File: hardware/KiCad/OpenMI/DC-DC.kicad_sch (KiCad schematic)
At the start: 37 parts, among them Q4 GAN7R0-150LBEZ, Q5 GAN7R0-150LBEZ, U3 1EDN7550B, U4 1EDN7550B

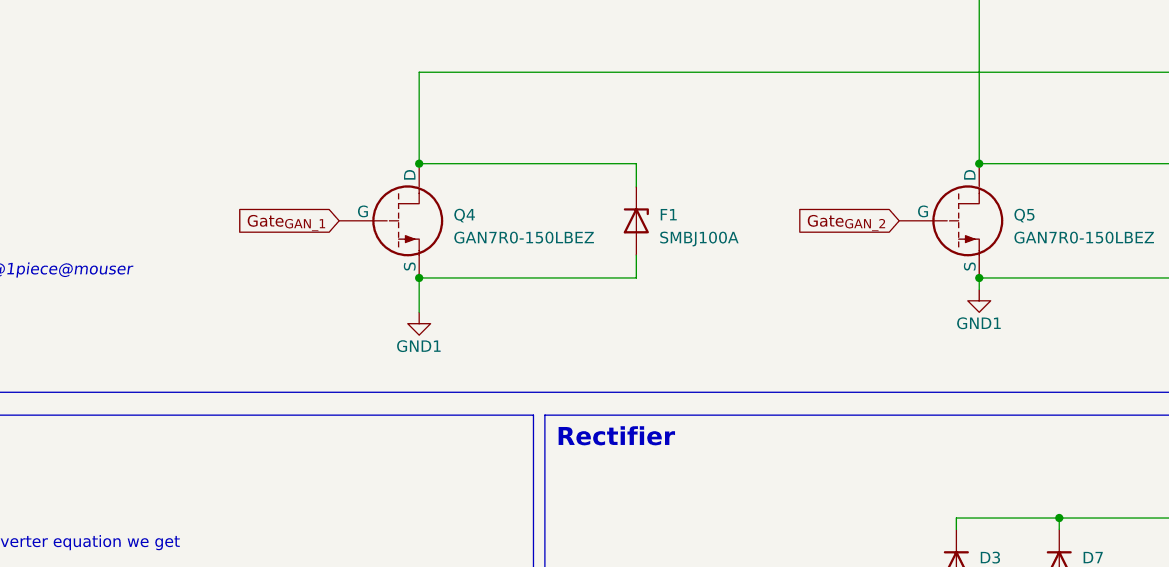
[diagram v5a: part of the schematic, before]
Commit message: feat(hw): adds safety resistors to gate of GaN FET
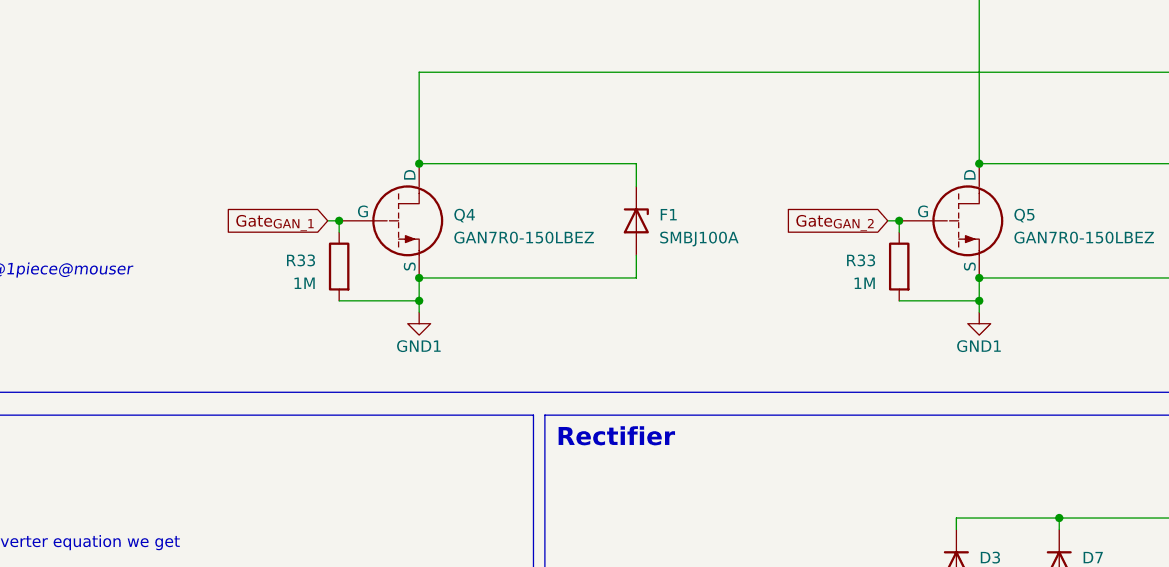
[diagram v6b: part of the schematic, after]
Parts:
- added R33 (x2): 1M, Resistor_SMD:R_0603_1608Metric, symbol _R_0603:1M
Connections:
- net GND1: now also R33.2, R33.2
- net Gate_{GAN_1}: now also R33.1
- net Gate_{GAN_2}: now also R33.1
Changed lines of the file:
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@@
   (junction (at 62.865 74.295) (diameter 0) (color 0 0 0 0)
   )
+  (junction (at 308.61 151.13) (diameter 0) (color 0 0 0 0)
+  )
   (junction (at 287.02 27.94) (diameter 0) (color 0 0 0 0)
   )
@@
   (junction (at 246.38 135.89) (diameter 0) (color 0 0 0 0)
   )
+  (junction (at 237.49 142.24) (diameter 0) (color 0 0 0 0)
+  )
   (junction (at 62.865 66.675) (diameter 0) (color 0 0 0 0)
   )
@@
   (junction (at 308.61 148.59) (diameter 0) (color 0 0 0 0)
   )
+  (junction (at 299.72 142.24) (diameter 0) (color 0 0 0 0)
+  )
   (junction (at 317.5 175.26) (diameter 0) (color 0 0 0 0)
   )
+  (junction (at 246.38 151.13) (diameter 0) (color 0 0 0 0)
+  )
   (junction (at 32.385 66.675) (diameter 0) (color 0 0 0 0)
   )
-  (wire (pts (xy 246.38 152.4) (xy 246.38 148.59))
+  (wire (pts (xy 308.61 152.4) (xy 308.61 151.13))
+    (stroke (width 0) (type default))
+  )
+  (wire (pts (xy 246.38 151.13) (xy 246.38 148.59))
+    (stroke (width 0) (type default))
+  )
+  (wire (pts (xy 246.38 152.4) (xy 246.38 151.13))
     (stroke (width 0) (type default))
   )
@@
     (stroke (width 0) (type default))
   )
+  (wire (pts (xy 236.22 142.24) (xy 237.49 142.24))
+    (stroke (width 0) (type default))
+  )
   (wire (pts (xy 265.43 90.17) (xy 275.59 90.17))
     (stroke (width 0) (type default))
@@
     (stroke (width 0) (type default))
   )
+  (wire (pts (xy 237.49 142.24) (xy 237.49 143.51))
+    (stroke (width 0) (type default))
+  )
   (wire (pts (xy 62.865 90.17) (xy 78.105 90.17))
     (stroke (width 0) (type default))
   )
+  (wire (pts (xy 298.45 142.24) (xy 299.72 142.24))
+    (stroke (width 0) (type default))
+  )
   (wire (pts (xy 331.47 175.26) (xy 331.47 184.15))
     (stroke (width 0) (type default))
@@
     (stroke (width 0) (type default))
   )
+  (wire (pts (xy 299.72 151.13) (xy 308.61 151.13))
+    (stroke (width 0) (type default))
+  )
   (wire (pts (xy 292.1 190.5) (xy 317.5 190.5))
     (stroke (width 0) (type default))
@@
     (stroke (width 0) (type default))
   )
+  (wire (pts (xy 237.49 151.13) (xy 246.38 151.13))
+    (stroke (width 0) (type default))
+  )
   (wire (pts (xy 311.15 50.8) (xy 317.5 50.8))
     (stroke (width 0) (type default))
@@
     (stroke (width 0) (type default))
   )
-  (wire (pts (xy 308.61 148.59) (xy 308.61 149.86))
+  (wire (pts (xy 308.61 148.59) (xy 308.61 151.13))
     (stroke (width 0) (type default))
   )
@@
   )
   (wire (pts (xy 47.625 74.295) (xy 62.865 74.295))
+    (stroke (width 0) (type default))
+  )
+  (wire (pts (xy 299.72 142.24) (xy 299.72 143.51))
     (stroke (width 0) (type default))
   )
@@
     )
   )
-  (global_label "Gate_{GAN_2}" (shape input) (at 299.72 142.24 180) (fields_autoplaced)
+  (global_label "Gate_{GAN_2}" (shape input) (at 298.45 142.24 180) (fields_autoplaced)
     (effects (font (size 1.27 1.27)) (justify right))
-    (property "Intersheetrefs" "${INTERSHEET_REFS}" (at 288.3984 142.24 0)
+    (property "Intersheetrefs" "${INTERSHEET_REFS}" (at 287.1284 142.24 0)
       (effects (font (size 1.27 1.27)) (justify right) hide)
     )
@@
     )
   )
-  (global_label "Gate_{GAN_1}" (shape input) (at 237.49 142.24 180) (fields_autoplaced)
+  (global_label "Gate_{GAN_1}" (shape input) (at 236.22 142.24 180) (fields_autoplaced)
     (effects (font (size 1.27 1.27)) (justify right))
-    (property "Intersheetrefs" "${INTERSHEET_REFS}" (at 226.1684 142.24 0)
+    (property "Intersheetrefs" "${INTERSHEET_REFS}" (at 224.8984 142.24 0)
       (effects (font (size 1.27 1.27)) (justify right) hide)
     )
@@
     )
   )
-  (symbol (lib_id "power:GND1") (at 308.61 149.86 0) (unit 1)
+  (symbol (lib_id "power:GND1") (at 308.61 152.4 0) (unit 1)
     (in_bom yes) (on_board yes) (dnp no)
-    (property "Reference" "#PWR028" (at 308.61 156.21 0)
-      (effects (font (size 1.27 1.27)) hide)
-    )
-    (property "Value" "GND1" (at 308.61 153.67 0)
-      (effects (font (size 1.27 1.27)))
-    )
-    (property "Footprint" "" (at 308.61 149.86 0)
-      (effects (font (size 1.27 1.27)) hide)
-    )
-    (property "Datasheet" "" (at 308.61 149.86 0)
+    (property "Reference" "#PWR028" (at 308.61 158.75 0)
+      (effects (font (size 1.27 1.27)) hide)
+    )
+    (property "Value" "GND1" (at 308.61 156.21 0)
+      (effects (font (size 1.27 1.27)))
+    )
+    (property "Footprint" "" (at 308.61 152.4 0)
+      (effects (font (size 1.27 1.27)) hide)
+    )
+    (property "Datasheet" "" (at 308.61 152.4 0)
       (effects (font (size 1.27 1.27)) hide)
     )
@@
     )
   )
+  (symbol (lib_id "_R_0603:1M") (at 299.72 147.32 0) (mirror y) (unit 1)
+    (in_bom yes) (on_board yes) (dnp no)
+    (property "Reference" "R33" (at 297.18 146.685 0)
+      (effects (font (size 1.27 1.27)) (justify left))
+    )
+    (property "Value" "1M" (at 297.18 149.225 0)
+      (effects (font (size 1.27 1.27)) (justify left))
+    )
+    (property "Footprint" "Resistor_SMD:R_0603_1608Metric" (at 301.498 147.32 90)
+      (effects (font (size 1.27 1.27)) hide)
+    )
+    (property "Datasheet" "~" (at 299.72 147.32 0)
+      (effects (font (size 1.27 1.27)) hide)
+    )
+    (property "MF" "" (at 299.72 147.32 0)
+      (effects (font (size 1.27 1.27)) hide)
+    )
+    (property "MPN" "" (at 299.72 147.32 0)
+      (effects (font (size 1.27 1.27)) hide)
+    )
+    (property "OC_CONRAD" "" (at 299.72 147.32 0)
+      (effects (font (size 1.27 1.27)) hide)
+    )
+    (property "OC_FARNELL" "" (at 299.72 147.32 0)
+      (effects (font (size 1.27 1.27)) hide)
+    )
+    (property "OC_MOUSER" "603-AC0603FR-071ML" (at 299.72 147.32 0)
+      (effects (font (size 1.27 1.27)) hide)
+    )
+    (property "OC_REICHELT" "" (at 299.72 147.32 0)
+      (effects (font (size 1.27 1.27)) hide)
+    )
+    (pin "1")
+    (pin "2")
+    (instances
+      (project "OpenMI"
+        (path "/2d959e19-1572-42a0-a8fd-da8463ad4e66/19323a41-9b99-4de4-bfae-f2f828815be3"
+          (reference "R33") (unit 1)
+        )
+        (path "/2d959e19-1572-42a0-a8fd-da8463ad4e66/efbfb180-c2bb-45aa-ab04-e5a4cb37fddc"
+          (reference "R37") (unit 1)
+        )
+      )
+    )
+  )
   (symbol (lib_name "33K_2") (lib_id "_R_0603:33K") (at 279.4 50.8 90) (unit 1)
     (in_bom yes) (on_board yes) (dnp no)
@@
         )
       )
+    )
+  )
+  (symbol (lib_id "_R_0603:1M") (at 237.49 147.32 0) (mirror y) (unit 1)
+    (in_bom yes) (on_board yes) (dnp no)
+    (property "Reference" "R33" (at 234.95 146.685 0)
+      (effects (font (size 1.27 1.27)) (justify left))
+    )
+    (property "Value" "1M" (at 234.95 149.225 0)
+      (effects (font (size 1.27 1.27)) (justify left))
+    )
+    (property "Footprint" "Resistor_SMD:R_0603_1608Metric" (at 239.268 147.32 90)
+      (effects (font (size 1.27 1.27)) hide)
+    )
+    (property "Datasheet" "~" (at 237.49 147.32 0)
+      (effects (font (size 1.27 1.27)) hide)
+    )
+    (property "MF" "" (at 237.49 147.32 0)
+      (effects (font (size 1.27 1.27)) hide)
+    )
+    (property "MPN" "" (at 237.49 147.32 0)
+      (effects (font (size 1.27 1.27)) hide)
+    )
+    (property "OC_CONRAD" "" (at 237.49 147.32 0)
+      (effects (font (size 1.27 1.27)) hide)
+    )
+    (property "OC_FARNELL" "" (at 237.49 147.32 0)
+      (effects (font (size 1.27 1.27)) hide)
+    )
+    (property "OC_MOUSER" "603-AC0603FR-071ML" (at 237.49 147.32 0)
+      (effects (font (size 1.27 1.27)) hide)
+    )
+    (property "OC_REICHELT" "" (at 237.49 147.32 0)
+      (effects (font (size 1.27 1.27)) hide)
+    )
+    (pin "1")
+    (pin "2")
+    (instances
+      (project "OpenMI"
+        (path "/2d959e19-1572-42a0-a8fd-da8463ad4e66/19323a41-9b99-4de4-bfae-f2f828815be3"
+          (reference "R33") (unit 1)
+        )
+        (path "/2d959e19-1572-42a0-a8fd-da8463ad4e66/efbfb180-c2bb-45aa-ab04-e5a4cb37fddc"
+          (reference "R36") (unit 1)
+        )
+      )

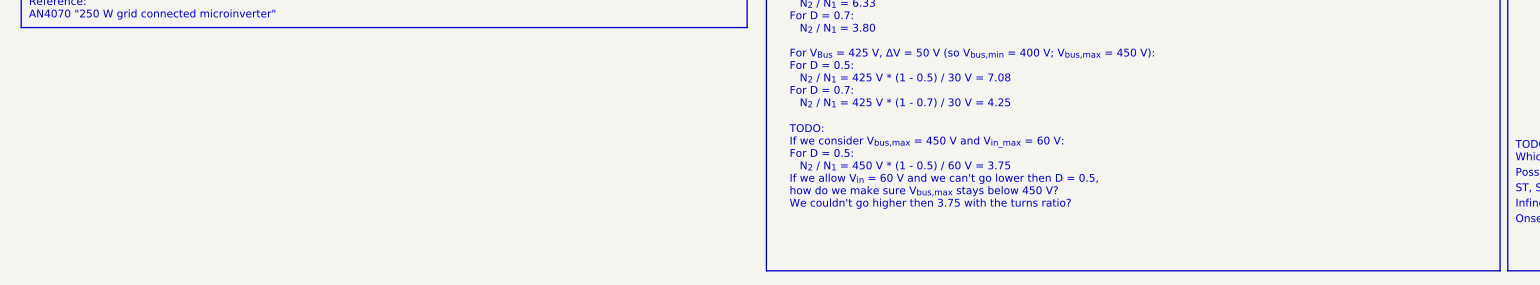
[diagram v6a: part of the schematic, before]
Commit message: chore: sync library for DC-DC schematic
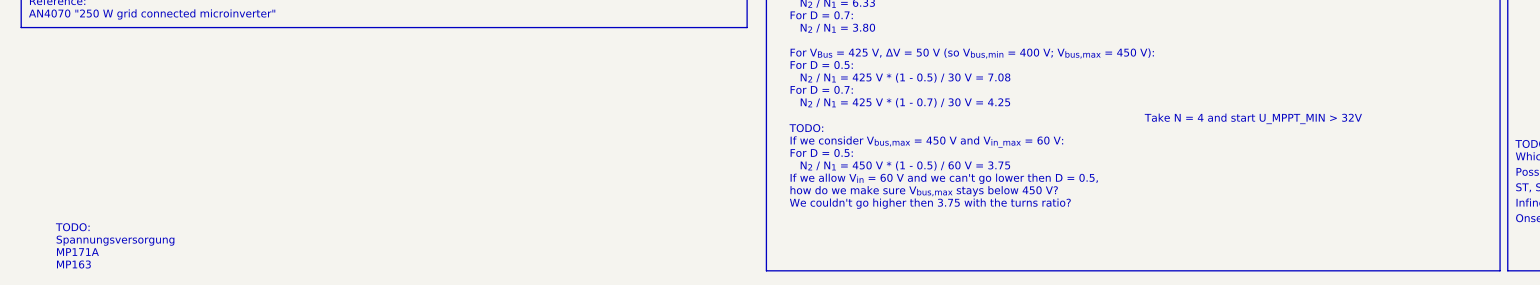
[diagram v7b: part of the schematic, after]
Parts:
- L3, L4, L5, L6, L7, L8: MF 60B104C -> Murata; MPN (none) -> 60B104C; OC_MOUSER 580-60B104C -> 580-60B104C
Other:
- note added: "TODO: Spannungsversorgung MP171A MP163"
- note added: "Take N = 4 and start U_MPPT_MIN > 32V"
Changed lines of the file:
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@@
     (effects (font (size 1.27 1.27) (thickness 0.254) bold) (justify left bottom))
+  )
+  (text "Take N = 4 and start U_MPPT_MIN > 32V" (at 200.66 212.09 0)
+    (effects (font (size 1.27 1.27) (color 255 0 0 1)) (justify left bottom))
   )
   (text "TODO:\nCapacitor size?" (at 340.36 190.5 0)
@@
     (at 18.415 23.495 0)
     (effects (font (size 1.27 1.27)) (justify left bottom))
+  )
+  (text "TODO:\nSpannungsversorgung\nMP171A \nMP163" (at 21.59 236.22 0)
+    (effects (font (size 1.27 1.27)) (justify left bottom) (href "https://www.monolithicpower.com/en/products/power-management/switching-converters-controllers/step-down-buck/converters/vin-max-48v.html"))
   )
   (text "Considerations about possible GaN FET driver:" (at 140.97 81.28 0)
@@
     )
   )
-  (symbol (lib_name "33K_1") (lib_id "_R_0603:33K") (at 279.4 45.72 90) (unit 1)
+  (symbol (lib_id "_R_0603:33K") (at 279.4 45.72 90) (unit 1)
     (in_bom yes) (on_board yes) (dnp no) (fields_autoplaced)
     (property "Reference" "R23" (at 279.4 40.64 90)
@@
       (effects (font (size 1.27 1.27)) hide)
     )
-    (property "MF" "60B104C" (at 105.41 123.19 0)
-      (effects (font (size 1.27 1.27)) hide)
-    )
-    (property "MPN" "" (at 105.41 123.19 0)
+    (property "MF" "Murata" (at 105.41 123.19 0)
+      (effects (font (size 1.27 1.27)) hide)
+    )
+    (property "MPN" "60B104C" (at 105.41 123.19 0)
       (effects (font (size 1.27 1.27)) hide)
     )
@@
       (effects (font (size 1.27 1.27)) hide)
     )
-    (property "OC_MOUSER" " 580-60B104C" (at 105.41 123.19 0)
+    (property "OC_MOUSER" "580-60B104C" (at 105.41 123.19 0)
       (effects (font (size 1.27 1.27)) hide)
     )
@@
       (effects (font (size 1.27 1.27)) hide)
     )
-    (property "MF" "60B104C" (at 119.38 113.665 0)
-      (effects (font (size 1.27 1.27)) hide)
-    )
-    (property "MPN" "" (at 119.38 113.665 0)
+    (property "MF" "Murata" (at 119.38 113.665 0)
+      (effects (font (size 1.27 1.27)) hide)
+    )
+    (property "MPN" "60B104C" (at 119.38 113.665 0)
       (effects (font (size 1.27 1.27)) hide)
     )
@@
       (effects (font (size 1.27 1.27)) hide)
     )
-    (property "OC_MOUSER" " 580-60B104C" (at 119.38 113.665 0)
+    (property "OC_MOUSER" "580-60B104C" (at 119.38 113.665 0)
       (effects (font (size 1.27 1.27)) hide)
     )
@@
     )
   )
-  (symbol (lib_name "33K_2") (lib_id "_R_0603:33K") (at 279.4 50.8 90) (unit 1)
+  (symbol (lib_id "_R_0603:33K") (at 279.4 50.8 90) (unit 1)
     (in_bom yes) (on_board yes) (dnp no)
     (property "Reference" "R24" (at 279.4 53.34 90)
@@
     )
   )
-  (symbol (lib_name "33K_3") (lib_id "_R_0603:33K") (at 279.4 90.17 90) (unit 1)
+  (symbol (lib_id "_R_0603:33K") (at 279.4 90.17 90) (unit 1)
     (in_bom yes) (on_board yes) (dnp no) (fields_autoplaced)
     (property "Reference" "R27" (at 279.4 85.09 90)
@@
       (effects (font (size 1.27 1.27)) hide)
     )
-    (property "MF" "60B104C" (at 91.44 113.665 0)
-      (effects (font (size 1.27 1.27)) hide)
-    )
-    (property "MPN" "" (at 91.44 113.665 0)
+    (property "MF" "Murata" (at 91.44 113.665 0)
+      (effects (font (size 1.27 1.27)) hide)
+    )
+    (property "MPN" "60B104C" (at 91.44 113.665 0)
       (effects (font (size 1.27 1.27)) hide)
     )
@@
       (effects (font (size 1.27 1.27)) hide)
     )
-    (property "OC_MOUSER" " 580-60B104C" (at 91.44 113.665 0)
+    (property "OC_MOUSER" "580-60B104C" (at 91.44 113.665 0)
       (effects (font (size 1.27 1.27)) hide)
     )
@@
       (effects (font (size 1.27 1.27)) hide)
     )
-    (property "MF" "60B104C" (at 119.38 123.19 0)
-      (effects (font (size 1.27 1.27)) hide)
-    )
-    (property "MPN" "" (at 119.38 123.19 0)
+    (property "MF" "Murata" (at 119.38 123.19 0)
+      (effects (font (size 1.27 1.27)) hide)
+    )
+    (property "MPN" "60B104C" (at 119.38 123.19 0)
       (effects (font (size 1.27 1.27)) hide)
     )
@@
       (effects (font (size 1.27 1.27)) hide)
     )
-    (property "OC_MOUSER" " 580-60B104C" (at 119.38 123.19 0)
+    (property "OC_MOUSER" "580-60B104C" (at 119.38 123.19 0)
       (effects (font (size 1.27 1.27)) hide)
     )
@@
     )
   )
-  (symbol (lib_name "33K_4") (lib_id "_R_0603:33K") (at 279.4 95.25 90) (unit 1)
+  (symbol (lib_id "_R_0603:33K") (at 279.4 95.25 90) (unit 1)
     (in_bom yes) (on_board yes) (dnp no)
     (property "Reference" "R28" (at 279.4 97.79 90)
@@
       (effects (font (size 1.27 1.27)) hide)
     )
-    (property "MF" "60B104C" (at 91.44 123.19 0)
-      (effects (font (size 1.27 1.27)) hide)
-    )
-    (property "MPN" "" (at 91.44 123.19 0)
+    (property "MF" "Murata" (at 91.44 123.19 0)
+      (effects (font (size 1.27 1.27)) hide)
+    )
+    (property "MPN" "60B104C" (at 91.44 123.19 0)
       (effects (font (size 1.27 1.27)) hide)
     )
@@
       (effects (font (size 1.27 1.27)) hide)
     )
-    (property "OC_MOUSER" " 580-60B104C" (at 91.44 123.19 0)
+    (property "OC_MOUSER" "580-60B104C" (at 91.44 123.19 0)
       (effects (font (size 1.27 1.27)) hide)
     )
@@
       (effects (font (size 1.27 1.27)) hide)
     )
-    (property "MF" "60B104C" (at 105.41 113.665 0)
-      (effects (font (size 1.27 1.27)) hide)
-    )
-    (property "MPN" "" (at 105.41 113.665 0)
+    (property "MF" "Murata" (at 105.41 113.665 0)
+      (effects (font (size 1.27 1.27)) hide)
+    )
+    (property "MPN" "60B104C" (at 105.41 113.665 0)
       (effects (font (size 1.27 1.27)) hide)
     )
@@
       (effects (font (size 1.27 1.27)) hide)
     )
-    (property "OC_MOUSER" " 580-60B104C" (at 105.41 113.665 0)
-      (effects (font (size 1.27 1.27)) hide)
-    )
+    (property "OC_MOUSER" "580-60B104C" (at 105.41 113.665 0)
+      (effects (font (size 1.27 1.27)) hide)
+    )

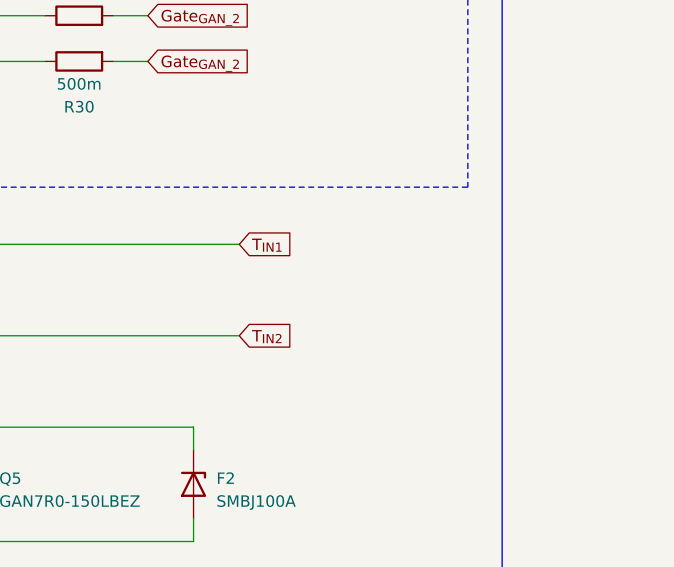
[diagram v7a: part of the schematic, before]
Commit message: docs(hw): adds todo on where to place transformer in schematic
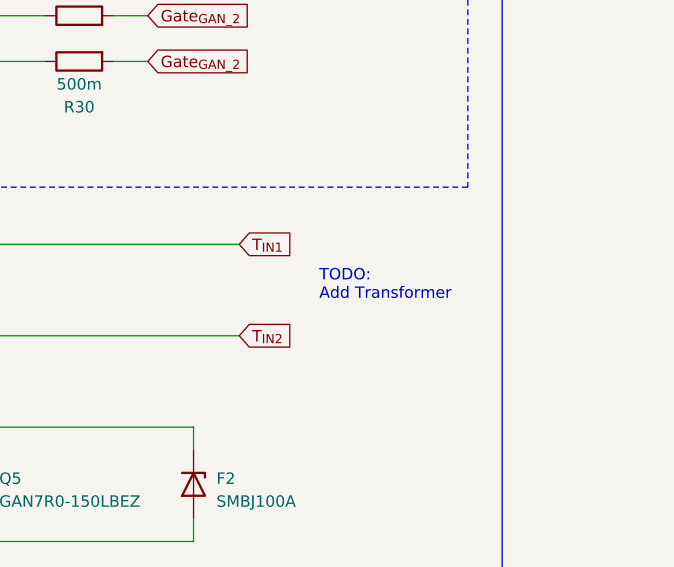
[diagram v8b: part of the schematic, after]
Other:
- note added: "TODO: Add Transformer"
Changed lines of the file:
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@@
     (effects (font (size 1.27 1.27)) (justify left bottom))
+  )
+  (text "TODO:\nAdd Transformer" (at 347.98 121.92 0)
+    (effects (font (size 1.27 1.27) (color 255 0 0 1)) (justify left bottom))
   )
   (text "Possible SiC diodes:\n" (at 261.62 220.98 0)
